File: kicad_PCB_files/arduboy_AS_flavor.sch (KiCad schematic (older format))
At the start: 112 parts, among them J1 SSD1306_SSH1106, J2 Expansion_port_NEW, J3 USB_B_Micro, Q1 2N7002, Q2 Si2301CDS, SW1 RST Button, SW2 UP Button, SW3 DOWN Button, SW4 LEFT Button, SW5 RIGHT Button, SW6 RIGHT Button, SW7 RIGHT Button, U1 ATmega32U4-MU, U1B1 ATmega32U4-AU, U2 W25Q128JVSIQ, U3 XC6206P33, U4 TP4054, U5 MPU-6050, Y1 16MHz

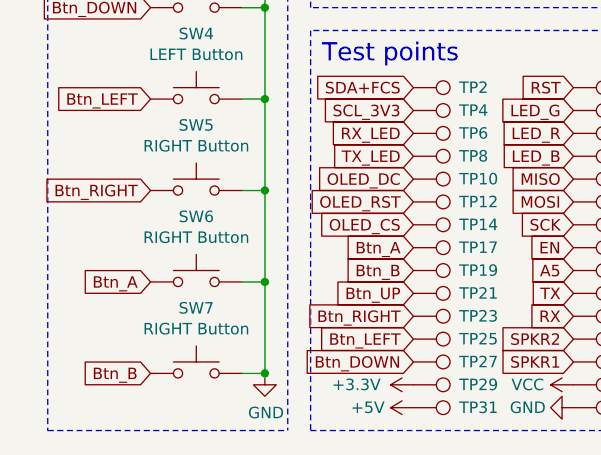
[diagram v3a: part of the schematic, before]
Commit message: PCB changes - Button footprints for clicky OR silent switches
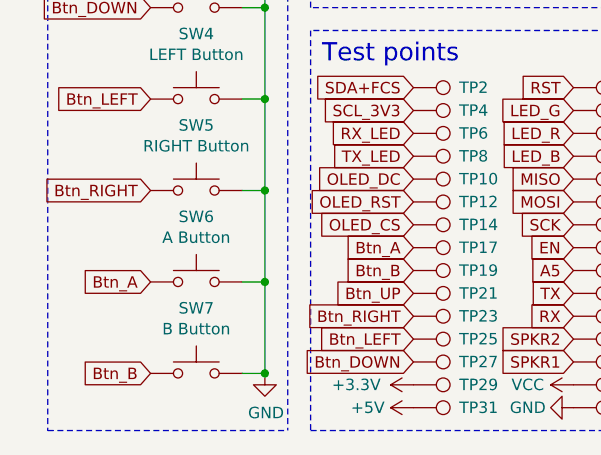
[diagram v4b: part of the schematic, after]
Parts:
- SW6: value RIGHT Button -> A Button
- SW7: value RIGHT Button -> B Button
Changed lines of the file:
@@
 P 1200 7050
 F 0 "SW6" H 1200 7335 50  0000 C CNN
-F 1 "RIGHT Button" H 1200 7244 50  0000 C CNN
+F 1 "A Button" H 1200 7244 50  0000 C CNN
 F 2 "arduboy:button_TS-1187A-B-A-B" H 1200 7250 50  0001 C CNN
 F 3 "~" H 1200 7250 50  0001 C CNN
@@
 P 1200 7450
 F 0 "SW7" H 1200 7735 50  0000 C CNN
-F 1 "RIGHT Button" H 1200 7644 50  0000 C CNN
+F 1 "B Button" H 1200 7644 50  0000 C CNN
 F 2 "arduboy:button_TS-1187A-B-A-B" H 1200 7650 50  0001 C CNN
 F 3 "~" H 1200 7650 50  0001 C CNN

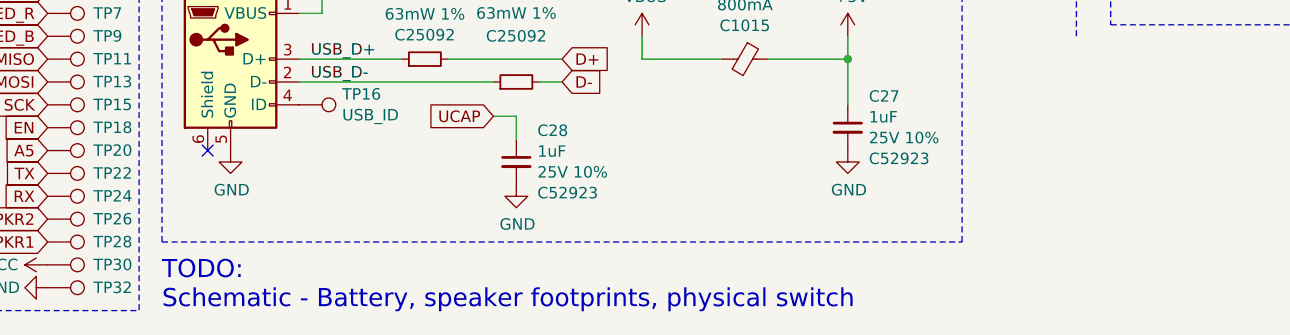
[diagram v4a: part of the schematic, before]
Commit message: Added mechanical mounting points Continued PCB placement feasibility
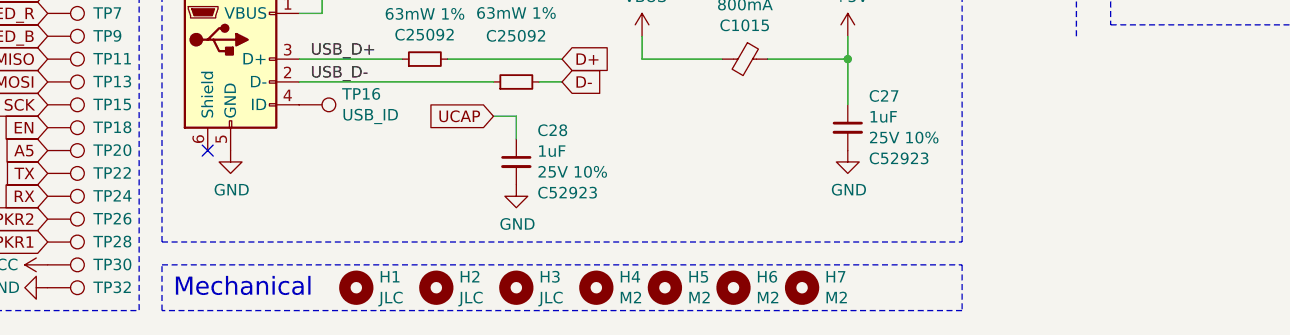
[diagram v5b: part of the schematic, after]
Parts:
- added H1, H2, H3: JLC, arduboy:JLCPCB_assembly_hole, symbol Mechanical:MountingHole
- added H4, H5, H6, H7: M2, arduboy:M2_mounting_hole, symbol Mechanical:MountingHole
- C1, C10, C11, C12, C13, C16, C17, C18, C19, C2, C20, C21, C22, C23, C24, C25, C26, C27, C28, C3, C4, C5, C6, C8, C9: footprint Capacitor_SMD:C_0402_1005Metric_Pad0.74x0.62mm_HandSolder -> no_refdes:0402_HandSolder
- C14, C15, C7: footprint Capacitor_SMD:C_0603_1608Metric_Pad1.08x0.95mm_HandSolder -> no_refdes:0603_HandSolder
- J1: footprint arduboy:SSH1106_30pin_P0.7mm -> arduboy:SSD1306_30pin_P0.7mm
- R1, R10, R11, R12, R13, R14, R16, R18, R19, R2, R20, R21, R3, R4, R5, R6, R7, R8, R9: footprint Resistor_SMD:R_0402_1005Metric_Pad0.72x0.64mm_HandSolder -> no_refdes:0402_HandSolder
- R15, R17: footprint Resistor_SMD:R_0603_1608Metric_Pad0.98x0.95mm_HandSolder -> no_refdes:0603_HandSolder
- SW1, SW2, SW3, SW4, SW5, SW6, SW7: LCSC (none) -> C318884
- Y1: footprint Crystal:Crystal_SMD_3225-4Pin_3.2x2.5mm_HandSoldering -> Crystal:Crystal_SMD_3225-4Pin_3.2x2.5mm
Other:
- note added: "Mechanical"
- note removed: "TODO:\nSchematic - Battery, speaker footprints, physical switch"

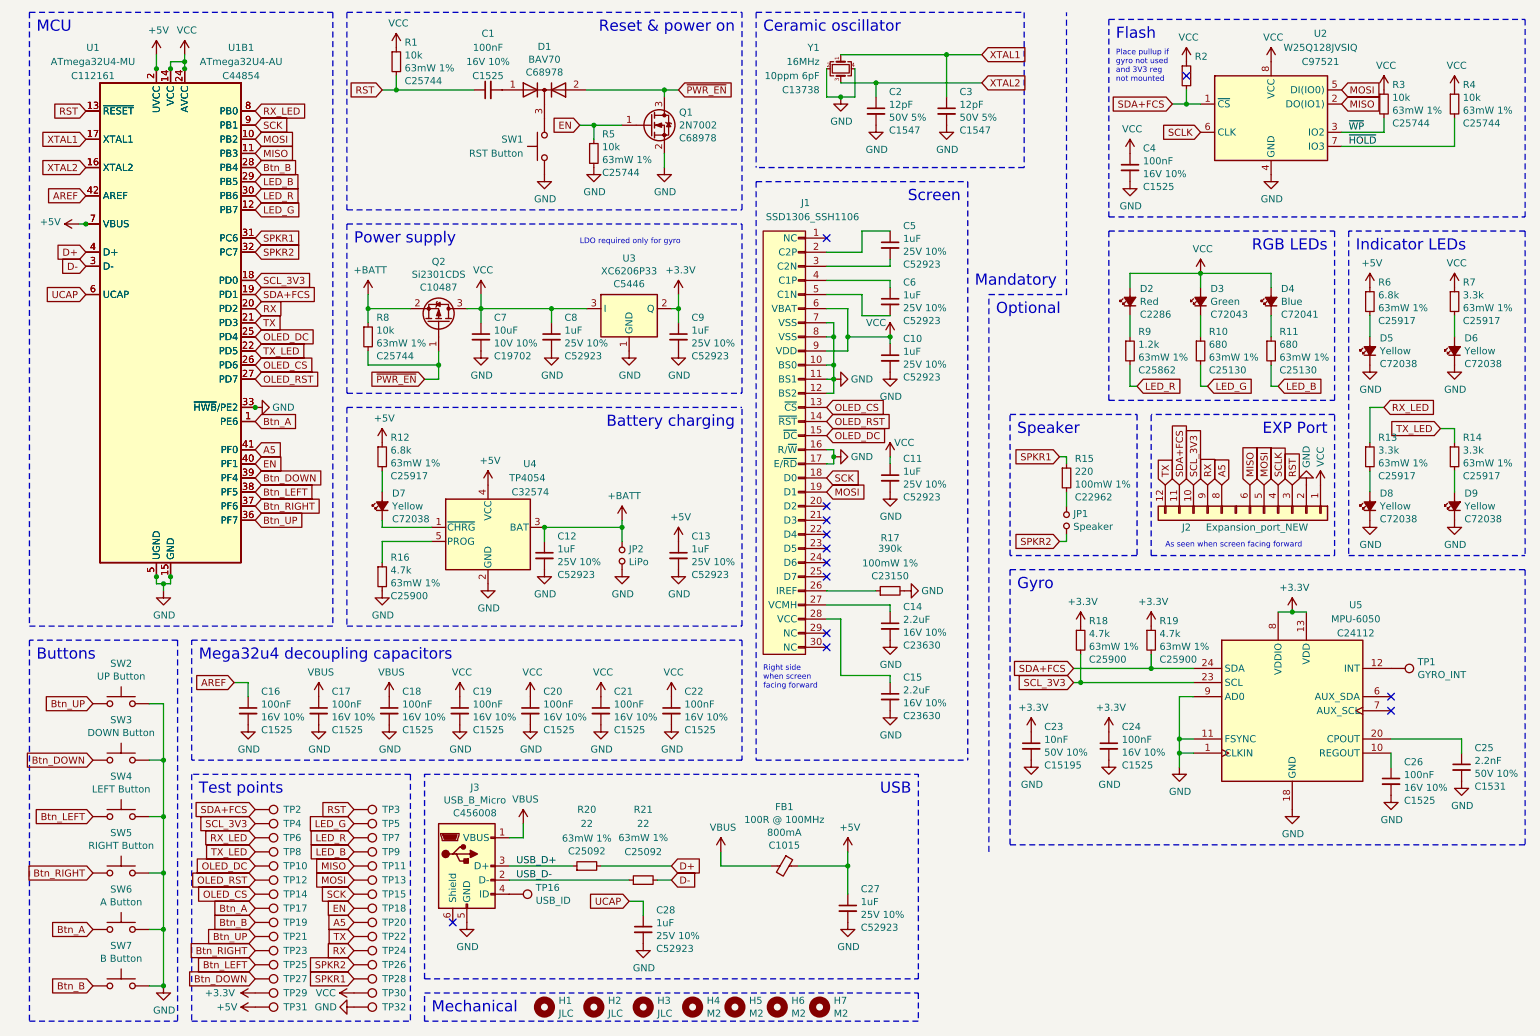
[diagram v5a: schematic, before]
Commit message: Changed reset circuit Continued PCB placement feasibility Changed piezo footprint
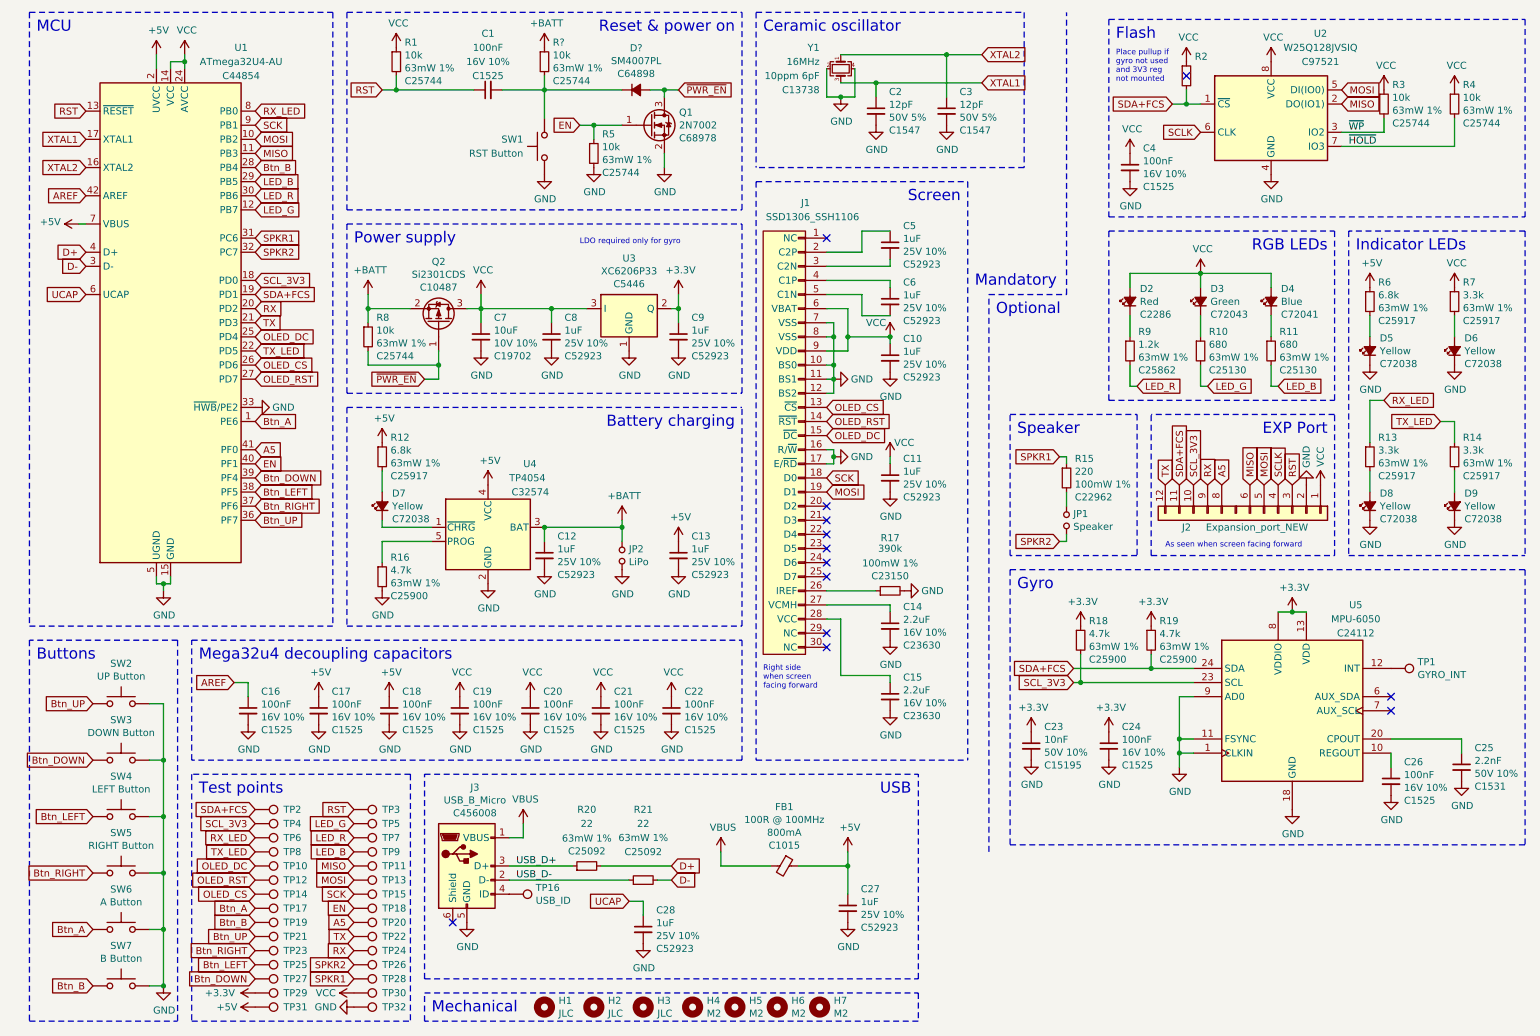
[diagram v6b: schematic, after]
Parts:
- removed D1: BAV70, Package_TO_SOT_SMD:SOT-23, symbol Diode:BAV70
- removed U1: ATmega32U4-MU, Package_DFN_QFN:QFN-44-1EP_7x7mm_P0.5mm_EP5.2x5.2mm, symbol MCU_Microchip_ATmega:ATmega32U4-MU
- added D?: SM4007PL, Diode_SMD:D_SOD-123F, symbol Device:D_Small_ALT
- added R?: 10k, no_refdes:0402_HandSolder, symbol Device:R_Small
- JP1: footprint Connector_PinHeader_2.54mm:PinHeader_1x02_P2.54mm_Vertical -> arduboy:CPT-12123-81-SMT
- renumbered U1B1 to U1
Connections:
- net +5V: now also C17.1, C18.1
- net +BATT: now also R?.1
- net VBUS: no longer C17.1, C18.1
- net XTAL1: now also C2.1, Y1.3; no longer C3.1, Y1.1
- net XTAL2: now also C3.1, Y1.1; no longer C2.1, Y1.3
- net ~PWR_EN: now also D?.2 (A)
- net at C1.2: now also SW1.2, D?.1 (K), R?.2
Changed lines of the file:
@@
 $EndDescr
 $Comp
-L MCU_Microchip_ATmega:ATmega32U4-AU U1B1
+L MCU_Microchip_ATmega:ATmega32U4-AU U1
 U 1 1 61600966
 P 1550 2750
-F 0 "U1B1" H 2050 4700 50  0000 C CNN
+F 0 "U1" H 2050 4700 50  0000 C CNN
 F 1 "ATmega32U4-AU" H 2050 4600 50  0000 C CNN
 F 2 "Package_QFP:TQFP-44_10x10mm_P0.8mm" H 1550 2750 50  0001 C CIN
@@
 $EndComp
 $Comp
-L MCU_Microchip_ATmega:ATmega32U4-MU U1
-U 1 1 61601C30
-P 1550 2750
-F 0 "U1" H 1000 4700 50  0000 C CNN
-F 1 "ATmega32U4-MU" H 1000 4600 50  0000 C CNN
-F 2 "Package_DFN_QFN:QFN-44-1EP_7x7mm_P0.5mm_EP5.2x5.2mm" H 1550 2750 50  0001 C CIN
-F 3 "http://ww1.microchip.com/downloads/en/DeviceDoc/Atmel-7766-8-bit-AVR-ATmega16U4-32U4_Datasheet.pdf" H 1550 2750 50  0001 C CNN
-F 4 "C112161" H 1000 4500 50  0000 C CNN "LCSC"
-	1    1550 2750
-	1    0    0    -1
-$EndComp
-$Comp
 L power:GND #PWR049
 U 1 1 615F3C57
@@
 Wire Wire Line
 	1500 4600 1500 4650
-Connection ~ 1450 4550
 Wire Wire Line
 	1500 4600 1550 4600
@@
 	1550 4600 1550 4550
 Connection ~ 1500 4600
-Connection ~ 1550 4550
 $Comp
 L Device:C_Small C28
@@
 	0    -1   -1   0
 $EndComp
-Connection ~ 950  2050
 Wire Wire Line
 	900  2050 950  2050
@@
 Text GLabel 950  1250 0    50   Input ~ 0
 RST
-Connection ~ 1450 950
 $Comp
 L power:VCC #PWR03
@@
 Wire Wire Line
 	1650 900  1650 950
-Connection ~ 1550 950
-Connection ~ 1650 950
 Wire Wire Line
 	1650 850  1650 900
@@
 	5100 6600 4600 6600
 $Comp
-L power:VBUS #PWR056
-U 1 1 6162E31A
-P 2600 5400
-F 0 "#PWR056" H 2600 5250 50  0001 C CNN
-F 1 "VBUS" H 2615 5573 50  0000 C CNN
-F 2 "" H 2600 5400 50  0001 C CNN
-F 3 "" H 2600 5400 50  0001 C CNN
-	1    2600 5400
-	1    0    0    -1
-$EndComp
-$Comp
 L Device:C_Small C17
 U 1 1 6162F4D4
@@
 $EndComp
 $Comp
-L power:VBUS #PWR057
-U 1 1 6163A3B6
-P 3100 5400
-F 0 "#PWR057" H 3100 5250 50  0001 C CNN
-F 1 "VBUS" H 3115 5573 50  0000 C CNN
-F 2 "" H 3100 5400 50  0001 C CNN
-F 3 "" H 3100 5400 50  0001 C CNN
-	1    3100 5400
-	1    0    0    -1
-$EndComp
-$Comp
 L Device:C_Small C18
 U 1 1 6163A3BE
@@
 Text GLabel 950  1650 0    50   Input ~ 0
 XTAL2
-Text GLabel 7300 850  2    50   Input ~ 0
-XTAL1
 Text GLabel 7300 1050 2    50   Input ~ 0
+XTAL1
+Text GLabel 7300 850  2    50   Input ~ 0
 XTAL2
 Text GLabel 950  2550 0    50   Input ~ 0
@@
 	9900 2100 9900 4400
 Wire Wire Line
-	10650 3500 10650 3600
-Wire Wire Line
-	10550 3500 10650 3500
-Wire Wire Line
-	10050 3350 10050 3600
-Wire Wire Line
-	10150 3350 10050 3350
+	10550 3450 10650 3450
 Wire Notes Line
 	9900 4400 11150 4400
@@
 Wire Wire Line
 	10050 3950 10050 3800
-Text GLabel 10550 3500 0    50   Input ~ 0
+Text GLabel 10550 3450 0    50   Input ~ 0
 TX_LED
-Text GLabel 10150 3350 2    50   Input ~ 0
+Text GLabel 10150 3300 2    50   Input ~ 0
 RX_LED
 Wire Notes Line
@@
 	1    0    0    -1
 $EndComp
-$Comp
-L Diode:BAV70 D1
-U 1 1 6175AACC
-P 4200 1100
-F 0 "D1" H 4200 1407 50  0000 C CNN
-F 1 "BAV70" H 4200 1316 50  0000 C CNN
-F 2 "Package_TO_SOT_SMD:SOT-23" H 4200 1100 50  0001 C CNN
-F 3 "https://assets.nexperia.com/documents/data-sheet/BAV70_SER.pdf" H 4200 1100 50  0001 C CNN
-F 4 "C68978" H 4200 1225 50  0000 C CNN "LCSC"
-	1    4200 1100
-	1    0    0    -1
-$EndComp
 Wire Wire Line
 	5050 1650 5050 1550
@@
 	0    -1   -1   0
 $EndComp
-Connection ~ 2150 3350
 Text GLabel 2150 2450 2    50   Input ~ 0
 SCL_3V3
@@
 	1    0    0    -1
 $EndComp
-$Comp
-L Device:R_Small R18
-U 1 1 61D8B1E4
-P 8000 5000
-F 0 "R18" H 8059 5137 50  0000 L CNN
-F 1 "4.7k" H 8059 5046 50  0000 L CNN
-F 2 "no_refdes:0402_HandSolder" H 8000 5000 50  0001 C CNN
-F 3 "~" H 8000 5000 50  0001 C CNN
-F 4 "63mW 1%" H 8059 4955 50  0000 L CNN "Rating"
-F 5 "C25900" H 8059 4864 50  0000 L CNN "LCSC"
-	1    8000 5000
-	1    0    0    -1
-$EndComp
 Wire Wire Line
 	8800 5200 8500 5200
@@
 Wire Wire Line
 	3150 1100 3700 1100
-Wire Wire Line
-	4500 1100 5050 1100
-Connection ~ 5050 1100
 Wire Notes Line style solid
 	5600 1950 5600 550
@@
 F 0 "JP1" V 7946 4102 50  0000 R CNN
 F 1 "Speaker" V 7855 4102 50  0000 R CNN
-F 2 "Connector_PinHeader_2.54mm:PinHeader_1x02_P2.54mm_Vertical" H 7900 4150 50  0001 C CNN
+F 2 "arduboy:CPT-12123-81-SMT" H 7900 4150 50  0001 C CNN
 F 3 "~" H 7900 4150 50  0001 C CNN
 	1    7900 4150
@@
 $EndComp
 $Comp
-L Device:C_Small C11
-U 1 1 61758A93
-P 6650 3850
-F 0 "C11" H 6742 3987 50  0000 L CNN
-F 1 "1uF" H 6742 3896 50  0000 L CNN
-F 2 "no_refdes:0402_HandSolder" H 6650 3850 50  0001 C CNN
-F 3 "~" H 6650 3850 50  0001 C CNN
-F 4 "25V 10%" H 6742 3805 50  0000 L CNN "Rating"
-F 5 "C52923" H 6742 3714 50  0000 L CNN "LCSC"
-	1    6650 3850
-	1    0    0    -1
-$EndComp
-$Comp
 L Device:C_Small C14
 U 1 1 616343ED
@@
 	1    0    0    -1
 $EndComp
+$Comp
+L power:+5V #PWR0101
+U 1 1 616CFDDB
+P 2600 5400
+F 0 "#PWR0101" H 2600 5250 50  0001 C CNN
+F 1 "+5V" H 2615 5573 50  0000 C CNN
+F 2 "" H 2600 5400 50  0001 C CNN
+F 3 "" H 2600 5400 50  0001 C CNN
+	1    2600 5400
+	1    0    0    -1
+$EndComp
+$Comp
+L power:+5V #PWR0102
+U 1 1 616D045F
+P 3100 5400
+F 0 "#PWR0102" H 3100 5250 50  0001 C CNN
+F 1 "+5V" H 3115 5573 50  0000 C CNN
+F 2 "" H 3100 5400 50  0001 C CNN
+F 3 "" H 3100 5400 50  0001 C CNN
+	1    3100 5400
+	1    0    0    -1
+$EndComp
+$Comp
+L Device:C_Small C11
+U 1 1 61758A93
+P 6650 3850
+F 0 "C11" H 6742 3987 50  0000 L CNN
+F 1 "1uF" H 6742 3896 50  0000 L CNN
+F 2 "no_refdes:0402_HandSolder" H 6650 3850 50  0001 C CNN
+F 3 "~" H 6650 3850 50  0001 C CNN
+F 4 "25V 10%" H 6742 3805 50  0000 L CNN "Rating"
+F 5 "C52923" H 6742 3714 50  0000 L CNN "LCSC"
+	1    6650 3850
+	1    0    0    -1
+$EndComp
+$Comp
+L Device:R_Small R18
+U 1 1 61D8B1E4
+P 8000 5000
+F 0 "R18" H 8059 5137 50  0000 L CNN
+F 1 "4.7k" H 8059 5046 50  0000 L CNN
+F 2 "no_refdes:0402_HandSolder" H 8000 5000 50  0001 C CNN
+F 3 "~" H 8000 5000 50  0001 C CNN
+F 4 "63mW 1%" H 8059 4955 50  0000 L CNN "Rating"
+F 5 "C25900" H 8059 4864 50  0000 L CNN "LCSC"
+	1    8000 5000
+	1    0    0    -1
+$EndComp
+Wire Wire Line
+	3900 1100 4200 1100
+Wire Wire Line
+	4200 1300 4200 1100
+Connection ~ 4200 1100
+Wire Wire Line
+	4200 1000 4200 1100
+$Comp
+L Device:R_Small R?
+U 1 1 61723BBB
+P 4200 900
+F 0 "R?" H 4259 1037 50  0000 L CNN
+F 1 "10k" H 4259 946 50  0000 L CNN
+F 2 "no_refdes:0402_HandSolder" H 4200 900 50  0001 C CNN
+F 3 "~" H 4200 900 50  0001 C CNN
+F 4 "63mW 1%" H 4259 855 50  0000 L CNN "Rating"
+F 5 "C25744" H 4259 764 50  0000 L CNN "LCSC"
+	1    4200 900
+	1    0    0    -1
+$EndComp
+$Comp
+L power:+BATT #PWR?
+U 1 1 6172BF3F
+P 4200 800
+F 0 "#PWR?" H 4200 650 50  0001 C CNN
+F 1 "+BATT" H 4215 973 50  0000 C CNN
+F 2 "" H 4200 800 50  0001 C CNN
+F 3 "" H 4200 800 50  0001 C CNN
+	1    4200 800
+	1    0    0    -1
+$EndComp
+$Comp
+L Device:D_Small_ALT D?
+U 1 1 6172D750
+P 4850 1100
+F 0 "D?" H 4850 1397 50  0000 C CNN
+F 1 "SM4007PL" H 4850 1306 50  0000 C CNN
+F 2 "Diode_SMD:D_SOD-123F" V 4850 1100 50  0001 C CNN
+F 3 "~" V 4850 1100 50  0001 C CNN
+F 4 "C64898" H 4850 1215 50  0000 C CNN "LCSC"
+	1    4850 1100
+	1    0    0    -1
+$EndComp
+Wire Wire Line
+	5050 1100 4950 1100
+Wire Wire Line
+	4750 1100 4200 1100
+Connection ~ 5050 1100
+Wire Wire Line
+	10650 3450 10650 3600
+Wire Wire Line
+	10150 3300 10050 3300
+Wire Wire Line
+	10050 3300 10050 3600
 $EndSCHEMATC
